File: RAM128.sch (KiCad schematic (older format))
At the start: 39 parts, among them J1 AppleIIBus, U1 621024, U10 74LS32, U11 74AHC1G126GW, U2 74HCT245, U3 74LS273, U4 74LS273, U5 74LS04, U6 74LS08, U7 74LS08, U8 74LS08, U9 74LS08

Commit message: Update docs
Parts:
- removed C12, C13, C14, C15, C16: 2u2, stdpads:C_0603, symbol Device:C_Small
- removed FID5: Fiducial, stdpads:Fiducial, symbol Mechanical:Fiducial
- removed H5: (no value), stdpads:PasteHole_1.1mm_PTH, symbol Mechanical:MountingHole_Pad
- C1: value 2u2 -> 10u; footprint stdpads:C_0805 -> stdpads:C_0603; LCSC Part (none) -> C23630
- C10, C2, C3, C4, C6, C7, C8, C9: LCSC Part (none) -> C23630
- C11: value 2u2 -> 10u; footprint stdpads:C_0603 -> stdpads:C_0805; LCSC Part (none) -> C15850
- C12: renamed from C5; value 2u2 -> 10u; LCSC Part (none) -> C15850
- R1: LCSC Part (none) -> C26010
- U1: LCSC Part (none) -> C261864
- U10: value 74LS32 -> 74HCT32; LCSC Part (none) -> C132266
- U11: LCSC Part (none) -> C7485
- U2: LCSC Part (none) -> C5980
- U3, U4: value 74LS273 -> 74HCT273; LCSC Part (none) -> C5983
- U5: value 74LS04 -> 74HCT04; LCSC Part (none) -> C131317
- U6, U7, U8, U9: value 74LS08 -> 74HCT08; LCSC Part (none) -> C8181
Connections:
- no-connect marks 7 -> 12
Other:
- moved on the sheet: C1, C10, C2, C3, C4, C6, C7, C8, C9, R1, U10B, U10C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

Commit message: Fabbed?
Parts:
- removed U2: 74HCT245, stdpads:TSSOP-20_4.4x6.5mm_P0.65mm, symbol 74xx:74HC245
- removed unit 2 of U7
- removed unit 1 of U7
- added H5: (no value), stdpads:PasteHole_1.152mm_NPTH, symbol Mechanical:MountingHole_Pad
- added U2: 74HCT245PW, stdpads:TSSOP-20_4.4x6.5mm_P0.65mm, symbol GW_Logic:74245
- added unit 1 of U7
- added unit 2 of U7
- C1: value 10u -> 2u2
- H1, H2, H3: footprint stdpads:PasteHole_1.1mm_PTH -> stdpads:PasteHole_1.152mm_NPTH
- U10: value 74HCT32 -> 74HCT32PW
- U11: value 74AHC1G126GW -> 74AHCT1G126GW
- U3, U4: value 74HCT273 -> 74HCT273PW
- U5: value 74HCT04 -> 74HCT04PW
- U6, U8, U9: value 74HCT08 -> 74HCT08PW
- U7: value 74HCT08 -> 74HCT32PW; symbol 74xx:74LS08 -> 74xx:74LS32
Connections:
- net +5V: now also U2.20 (Vcc)
- net A0: now also U6.13
- net A1: now also U6.5; no longer U6.2
- net A2: now also U7.4; no longer U6.9
- net D0: now also U2.11 (B7)
- net D1: now also U2.12 (B6)
- net D2: now also U2.13 (B5)
- net D3: now also U2.14 (B4)
- net D4: now also U2.15 (B3)
- net D5: now also U2.16 (B2)
- net D6: now also U2.17 (B1)
- net D7: now also U2.18 (B0)
- net ENWR1: now also U6.12
- net ENWR1A0: now also U6.11
- net GND: now also U6.10, U6.9, H5.1, U2.10 (GND)
- net RD0: now also U2.5 (A3)
- net RD1: now also U2.4 (A2)
- net RD2: now also U2.3 (A1)
- net RD3: now also U2.2 (A0)
- net RD4: now also U2.9 (A7)
- net RD5: now also U2.8 (A6)
- net RD6: now also U2.7 (A5)
- net RD7: now also U2.6 (A4)
- net R~CS~: now also U2.19 (~OE~)
- net ~DEVSEL~: now also U7.2, U7.5; no longer U6.10, U6.13
- net at U5.6: now also U7.1; no longer U6.12
- net at U5.4: now also U6.2; no longer U6.5
- net R~WE~ renamed R~W~
- net R~W~: now also U2.1 (AtoB)
- net ~DEV~andA2: no longer names the net of U6.8
- net ~DEV~andA2: no longer U4.11 (Cp)
- net ~DEV~and~A2~ renamed ~A2~clk
- net ~A2~clk: now also U7.6; no longer U6.11
- new net A2clk: U4.11 (Cp), U7.3
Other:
- moved on the sheet: C1, C10, C11, C12, C2, C3, C4, C6, C7, C8, C9, FID1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

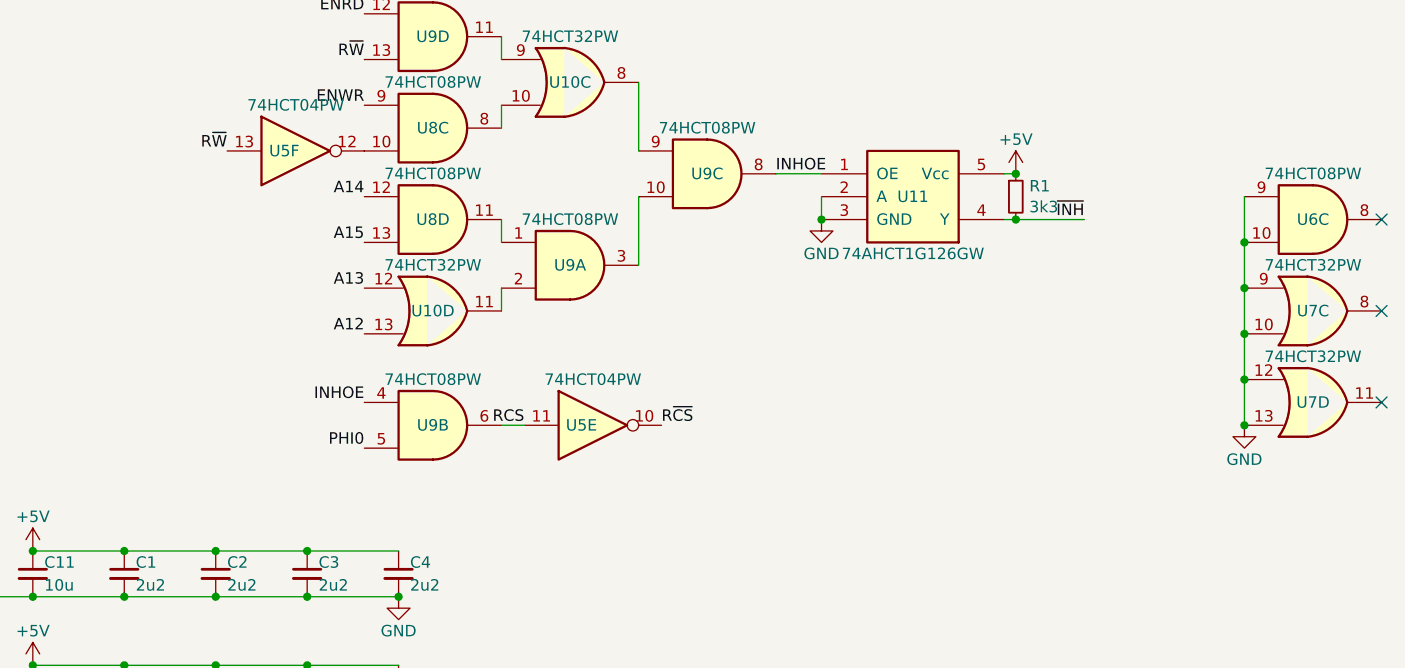
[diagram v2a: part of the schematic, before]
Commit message: DMA_OUT change
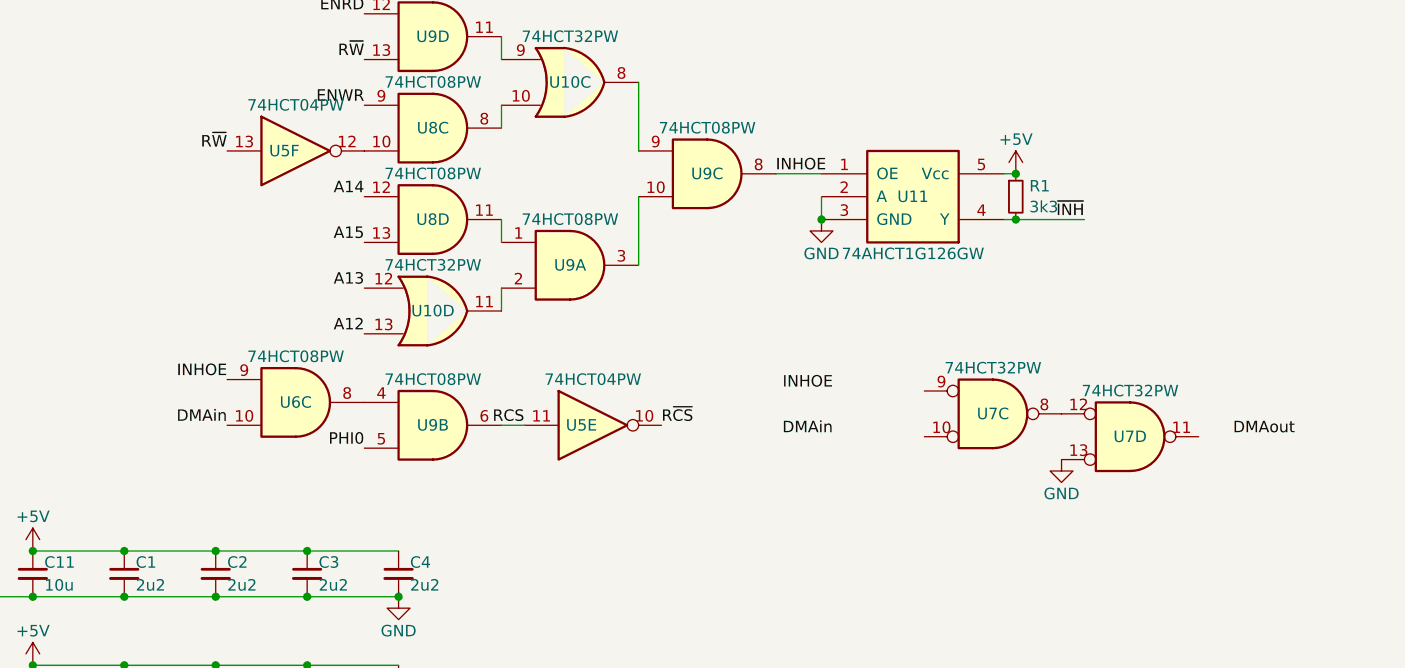
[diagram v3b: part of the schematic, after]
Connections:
- net DMAin: now also U6.10
- net GND: no longer U6.10, U6.9, U7.10, U7.12, U7.9
- net INHOE: now also U6.9; no longer U9.4
- net at U7.8: now also U7.12
- net at U6.8: now also U9.4
- no-connect marks 12 -> 9
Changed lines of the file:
@@
 Wire Bus Line
 	1850 4450 650  4450
-Text Label 8950 5300 2    50   ~ 0
-~INH~
 Text Label 5800 4600 2    50   ~ 0
 R~W~
@@
 	1    0    0    -1
 $EndComp
-Wire Wire Line
-	8650 5300 8950 5300
 $Comp
 L power:GND #PWR0126
@@
 Wire Wire Line
 	8650 5300 8600 5300
-Connection ~ 8650 5300
 $Comp
 L GW_Logic:741G126GW U11
@@
 Wire Wire Line
 	7800 5100 7600 5100
-Text Label 5800 6100 2    50   ~ 0
+Text Label 7850 6050 2    50   ~ 0
 INHOE
 Text Label 5800 5200 2    50   ~ 0
@@
 	1    0    0    -1
 $EndComp
-$Comp
-L 74xx:74LS32 U7
-U 3 1 5FD0EE1D
-P 9950 5700
-F 0 "U7" H 9950 5700 50  0000 C CNN
-F 1 "74HCT32PW" H 9950 5900 50  0000 C CNN
-F 2 "stdpads:TSSOP-14_4.4x5mm_P0.65mm" H 9950 5700 50  0001 C CNN
-F 3 "http://www.ti.com/lit/gpn/sn74LS08" H 9950 5700 50  0001 C CNN
-F 4 "C8181" H 9950 5700 50  0001 C CNN "LCSC Part"
-	3    9950 5700
-	1    0    0    -1
-$EndComp
-$Comp
-L 74xx:74LS32 U7
-U 4 1 5FD11853
-P 9950 6100
-F 0 "U7" H 9950 6100 50  0000 C CNN
-F 1 "74HCT32PW" H 9950 6300 50  0000 C CNN
-F 2 "stdpads:TSSOP-14_4.4x5mm_P0.65mm" H 9950 6100 50  0001 C CNN
-F 3 "http://www.ti.com/lit/gpn/sn74LS08" H 9950 6100 50  0001 C CNN
-F 4 "C8181" H 9950 6100 50  0001 C CNN "LCSC Part"
-	4    9950 6100
-	1    0    0    -1
-$EndComp
-$Comp
-L power:GND #PWR0127
-U 1 1 5FD15737
-P 9650 6200
-F 0 "#PWR0127" H 9650 5950 50  0001 C CNN
-F 1 "GND" H 9650 6050 50  0000 C CNN
-F 2 "" H 9650 6200 50  0001 C CNN
-F 3 "" H 9650 6200 50  0001 C CNN
-	1    9650 6200
-	1    0    0    -1
-$EndComp
-Wire Wire Line
-	9650 6200 9650 6000
-Connection ~ 9650 6200
-Connection ~ 9650 5800
-Wire Wire Line
-	9650 5800 9650 5600
-Connection ~ 9650 6000
-Wire Wire Line
-	9650 6000 9650 5800
-NoConn ~ 10250 5700
-NoConn ~ 10250 6100
 Wire Wire Line
 	8400 3050 8400 3150
@@
 	1    0    0    -1
 $EndComp
-$Comp
-L 74xx:74LS08 U6
-U 3 1 61A057BE
-P 9950 5300
-F 0 "U6" H 9950 5300 50  0000 C CNN
-F 1 "74HCT08PW" H 9950 5500 50  0000 C CNN
-F 2 "stdpads:TSSOP-14_4.4x5mm_P0.65mm" H 9950 5300 50  0001 C CNN
-F 3 "http://www.ti.com/lit/gpn/sn74LS08" H 9950 5300 50  0001 C CNN
-F 4 "C8181" H 9950 5300 50  0001 C CNN "LCSC Part"
-	3    9950 5300
-	1    0    0    -1
-$EndComp
-Wire Wire Line
-	9650 5200 9650 5400
-Wire Wire Line
-	9650 5400 9650 5600
-Connection ~ 9650 5400
-Connection ~ 9650 5600
 Wire Wire Line
 	7200 2150 7200 2350
-NoConn ~ 10250 5300
 Text Label 8000 2050 2    50   ~ 0
 ~DEVSEL~
@@
 Wire Bus Line
 	4550 2200 1750 2200
+$Comp
+L 74xx:74LS08 U6
+U 3 1 62D8945C
+P 5500 6100
+F 0 "U6" H 5500 6100 50  0000 C CNN
+F 1 "74HCT08PW" H 5500 6300 50  0000 C CNN
+F 2 "stdpads:TSSOP-14_4.4x5mm_P0.65mm" H 5500 6100 50  0001 C CNN
+F 3 "http://www.ti.com/lit/gpn/sn74LS08" H 5500 6100 50  0001 C CNN
+F 4 "C8181" H 5500 6100 50  0001 C CNN "LCSC Part"
+	3    5500 6100
+	1    0    0    -1
+$EndComp
+Text Label 5200 6200 2    50   ~ 0
+DMAin
+Text Label 9600 6250 0    50   ~ 0
+DMAout
+$Comp
+L 74xx:74LS32 U7
+U 3 2 62D952DF
+P 8550 6150
+F 0 "U7" H 8550 6150 50  0000 C CNN
+F 1 "74HCT32PW" H 8550 6350 50  0000 C CNN
+F 2 "stdpads:TSSOP-14_4.4x5mm_P0.65mm" H 8550 6150 50  0001 C CNN
+F 3 "http://www.ti.com/lit/gpn/sn74LS08" H 8550 6150 50  0001 C CNN
+F 4 "C8181" H 8550 6150 50  0001 C CNN "LCSC Part"
+	3    8550 6150
+	1    0    0    -1
+$EndComp
+$Comp
+L 74xx:74LS32 U7
+U 4 2 62D9A4DE
+P 9150 6250
+F 0 "U7" H 9150 6250 50  0000 C CNN
+F 1 "74HCT32PW" H 9150 6450 50  0000 C CNN
+F 2 "stdpads:TSSOP-14_4.4x5mm_P0.65mm" H 9150 6250 50  0001 C CNN
+F 3 "http://www.ti.com/lit/gpn/sn74LS08" H 9150 6250 50  0001 C CNN
+F 4 "C8181" H 9150 6250 50  0001 C CNN "LCSC Part"
+	4    9150 6250
+	1    0    0    -1
+$EndComp
+Connection ~ 8650 5300
+Wire Wire Line
+	8650 5300 8950 5300
+Text Label 8950 5300 2    50   ~ 0
+~INH~
+Text Label 5200 6000 2    50   ~ 0
+INHOE
+$Comp
+L power:GND #PWR?
+U 1 1 62DFF365
+P 8850 6350
+F 0 "#PWR?" H 8850 6100 50  0001 C CNN
+F 1 "GND" H 8850 6200 50  0000 C CNN
+F 2 "" H 8850 6350 50  0001 C CNN
+F 3 "" H 8850 6350 50  0001 C CNN
+	1    8850 6350
+	1    0    0    -1
+$EndComp
+Text Label 7850 6250 2    50   ~ 0
+DMAin
 Wire Bus Line
 	3150 2650 3150 3350

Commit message: done with little logic
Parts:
- removed U10, U7: 74HCT32PW, stdpads:TSSOP-14_4.4x5mm_P0.65mm, symbol 74xx:74LS32
- removed U5: 74HCT04PW, stdpads:TSSOP-14_4.4x5mm_P0.65mm, symbol 74xx:74LS04
- removed U6, U8, U9: 74HCT08PW, stdpads:TSSOP-14_4.4x5mm_P0.65mm, symbol 74xx:74LS08
- added JP1: Disable DMA Gate, Connector_PinHeader_2.54mm:PinHeader_1x02_P2.54mm_Vertical, symbol Device:Jumper_NO_Small
- added R3, R4: 30, stdpads:R_0603, symbol Device:R_Small
- added R6: 3k3, stdpads:R_0603, symbol Device:R_Small
- added U10, U15, U17, U18, U20, U25, U29, U31, U33: 742G04GW, stdpads:SOT-363, symbol GW_Logic:742G04GW
- added U12, U14, U19, U22, U23, U24, U26, U27, U28, U30, U5, U7, U9: 74LVC1G08GW, stdpads:SOT-353, symbol GW_Logic:741G02GW
- added U13, U16, U21, U32, U34, U6, U8: 74LVC1G32GW, stdpads:SOT-353, symbol GW_Logic:741G02GW
- added U35: XC6206PxxxMR, stdpads:SOT-23, symbol Regulator_Linear:XC6206PxxxMR
- R1: footprint stdpads:R_0805 -> stdpads:R_0603
- U1: footprint stdpads:TSOP-I-32_18.4x8mm_P0.5mm -> stdpads:TSOP-I-32_11.8x8mm_P0.5mm; LCSC Part C261864 -> (none)
- U11: value 74AHCT1G126GW -> 74LVC1G125GW; symbol GW_Logic:741G126GW -> GW_Logic:741G125GW
- U2: value 74HCT245PW -> 74AHC245PW; LCSC Part C426701 -> (none)
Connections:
- net +5V: now also U35.3 (VI); no longer C10.1, C2.1, C3.1, C4.1, C6.1, C7.1, C8.1, C9.1, R1.1, U1.6 (CS), U1.8 (VCC), U11.5 (Vcc), U2.20 (Vcc), U3.20 (VCC), U4.20 (VCC)
- net A0: now also U10.1 (1A), U7.1 (B), U9.2 (A); no longer U1.1 (A11)
- net A1: now also U10.3 (2A), U7.2 (A); no longer U1.2 (A9)
- net A10: now also U25.1 (1A); no longer U1.19 (A1)
- net A11: now also U25.3 (2A); no longer U1.20 (A0)
- net A12: now also U12.2 (A), U32.2 (A)
- net A13: now also U29.1 (1A), U32.1 (B); no longer U1.31 (A10)
- net A14: now also U26.1 (B)
- net A15: now also U26.2 (A)
- net A2: now also U15.1 (1A), U16.1 (B); no longer U1.3 (A8)
- net A2clk: now also U8.4 (Y)
- net A3: now also U15.3 (2A); no longer U1.4 (A13)
- net A4: now also U17.1 (1A); no longer U1.16 (A4)
- net A5: now also U17.3 (2A); no longer U1.15 (A5)
- net A6: now also U18.1 (1A); no longer U1.13 (A7)
- net A7: now also U18.3 (2A); no longer U1.7 (A15)
- net A8: now also U20.1 (1A); no longer U1.17 (A3)
- net A9: now also U20.3 (2A); no longer U1.18 (A2)
- net BankAB: now also U14.2 (A)
- net DMAin: now also U22.2 (A), U27.2 (A); no longer J1.24 (Pin_24)
- net ENRD: now also U19.1 (B)
- net ENWR: now also U23.1 (B)
- net ENWR1: now also U9.1 (B)
- net ENWR1A0: now also U9.4 (Y)
- net GND: now also R6.2, U10.2 (GND), U12.3 (GND), U13.3 (GND), U14.3 (GND), U15.2 (GND), U16.3 (GND), U17.2 (GND), U18.2 (GND), U19.3 (GND), U20.2 (GND), U21.3 (GND), U22.3 (GND), U23.3 (GND), U24.3 (GND), U25.2 (GND), U26.3 (GND), U27.3 (GND), U28.3 (GND), U29.2 (GND), U30.3 (GND), U31.2 (GND), U32.3 (GND), U33.2 (GND), U34.3 (GND), U35.1 (GND), U5.3 (GND), U6.3 (GND), U7.3 (GND), U8.3 (GND), U9.3 (GND); no longer U3.17 (D6)
- net INHOE: now also U24.4 (Y), U27.1 (B), U31.1 (1A); no longer U11.1 (OE)
- net PHI0: now also U30.2 (A)
- net RA12: now also U1.1 (A11), U13.4 (Y); no longer U1.14 (A6)
- net RA14: now also U1.16 (A4); no longer U1.12 (A12)
- net RA15: now also U1.15 (A5); no longer U1.11 (A14)
- net RA16: now also U1.14 (A6); no longer U1.10 (A16)
- net RCS: now also U30.4 (Y), U31.3 (2A)
- net R~CS~: now also U31.4 (2Y)
- net R~W~: now also U33.3 (2A); no longer U1.5 (~WE), U2.1 (AtoB)
- net ~A0XOR1~: now also U6.4 (Y)
- net ~A2~clk: now also U16.4 (Y)
- net ~DEVSEL~: now also U16.2 (A), U8.2 (A)
- net ~INH~: now also R4.1; no longer R1.2, U11.4 (Y)
- new net: R1.2, R4.2, U11.4 (Y)
- new net: U5.4 (Y), U6.2 (A)
- new net: U6.1 (B), U7.4 (Y)
- new net: U12.4 (Y), U13.2 (A)
- new net: U13.1 (B), U14.4 (Y)
- new net: U19.4 (Y), U21.1 (B)
- new net: U21.2 (A), U23.4 (Y)
- new net: U21.4 (Y), U24.1 (B)
- new net: U26.4 (Y), U28.2 (A)
- new net: U28.1 (B), U32.4 (Y)
- new net: U24.2 (A), U28.4 (Y)
- new net: U27.4 (Y), U30.1 (B)
- new net: U22.1 (B), U34.4 (Y)
- new net: R3.2, U22.4 (Y)
- new net: JP1.2, R6.1, U34.2 (A)
- new net +3V3: C10.1, C2.1, C3.1, C4.1, C6.1, C7.1, C8.1, C9.1, JP1.1, R1.1, U1.6 (CS), U1.8 (VCC), U10.5 (Vcc), U11.5 (Vcc), U12.5 (Vcc), U13.5 (Vcc), U14.5 (Vcc), U15.5 (Vcc), U16.5 (Vcc), U17.5 (Vcc), U18.5 (Vcc), U19.5 (Vcc), U2.20 (Vcc), U20.5 (Vcc), U21.5 (Vcc), U22.5 (Vcc), U23.5 (Vcc), U24.5 (Vcc), U25.5 (Vcc), U26.5 (Vcc), U27.5 (Vcc), U28.5 (Vcc), U29.5 (Vcc), U3.17 (D6), U3.20 (VCC), U30.5 (Vcc), U31.5 (Vcc), U32.5 (Vcc), U33.5 (Vcc), U34.5 (Vcc), U35.2 (VO), U4.20 (VCC), U5.5 (Vcc), U6.5 (Vcc), U7.5 (Vcc), U8.5 (Vcc), U9.5 (Vcc)
- new net DMAout: J1.24 (Pin_24), R3.1
- new net RA13: U1.2 (A9), U12.1 (B), U29.4 (2Y)
- new net RR~W~: U1.5 (~WE), U19.2 (A), U2.1 (AtoB), U33.6 (1Y)
- new net R~R~W: U23.2 (A), U33.1 (1A), U33.4 (2Y)
- new net ~A0: U1.31 (A10), U10.6 (1Y), U5.1 (B)
- new net ~A1: U1.20 (A0), U10.4 (2Y), U5.2 (A)
- new net ~A10: U1.4 (A13), U25.6 (1Y)
- new net ~A11: U1.3 (A8), U25.4 (2Y)
- new net ~A13: U14.1 (B), U29.3 (2A), U29.6 (1Y)
- new net ~A2: U1.19 (A1), U15.6 (1Y), U8.1 (B)
- new net ~A3: U1.18 (A2), U15.4 (2Y)
- new net ~A4: U1.17 (A3), U17.6 (1Y)
- new net ~A5: U1.13 (A7), U17.4 (2Y)
- new net ~A6: U1.12 (A12), U18.6 (1Y)
- new net ~A7: U1.11 (A14), U18.4 (2Y)
- new net ~A8: U1.10 (A16), U20.6 (1Y)
- new net ~A9: U1.7 (A15), U20.4 (2Y)
- new net ~INHOE~: U11.1 (~OE~), U31.6 (1Y), U34.1 (B)
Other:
- moved on the sheet: R1

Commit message: little logic done
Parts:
- added C13, C14, C15, C16, C17, C18, C19, C5: 2u2, stdpads:C_0603, symbol Device:C_Small
- added R2: 33, stdpads:R_0603, symbol Device:R_Small
- R1: LCSC Part C26010 -> C22978
- R3, R4: value 30 -> 33; LCSC Part (none) -> C23140
- R6: LCSC Part (none) -> C22978
- U1: value 621024 -> LY62W1024; LCSC Part (none) -> C261880
- U10, U15, U17, U18, U20, U25, U29, U31, U33: value 742G04GW -> 74LVC2G04GW; LCSC Part (none) -> C105251
- U12, U14, U19, U22, U23, U24, U26, U27, U28, U30, U5, U7, U9: LCSC Part (none) -> C12490
- U13, U16, U21, U32, U34, U6, U8: LCSC Part (none) -> C12489
- U2: LCSC Part (none) -> C132987
- U35: LCSC Part (none) -> C5446
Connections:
- net +3V3: now also C1.1, C13.1, C14.1, C15.1, C16.1, C17.1, C18.1, C19.1, C5.1
- net +5V: no longer C1.1
- net GND: now also C13.2, C14.2, C15.2, C16.2, C17.2, C18.2, C19.2, C5.2
- net R~CS~: now also R2.1; no longer U31.4 (2Y)
- new net: R2.2, U31.4 (2Y)
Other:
- moved on the sheet: C1, C10, C11, C12, C2, C3, C4, C6, C7, C8, C9, FID1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

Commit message: Revert "little logic done"
This reverts commit c8f7fd6b2897fba301a82931860b3ed280e7265e.
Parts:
- removed C13, C14, C15, C16, C17, C18, C19, C5: 2u2, stdpads:C_0603, symbol Device:C_Small
- removed R2: 33, stdpads:R_0603, symbol Device:R_Small
- R1: LCSC Part C22978 -> C26010
- R3, R4: value 33 -> 30; LCSC Part C23140 -> (none)
- R6: LCSC Part C22978 -> (none)
- U1: value LY62W1024 -> 621024; LCSC Part C261880 -> (none)
- U10, U15, U17, U18, U20, U25, U29, U31, U33: value 74LVC2G04GW -> 742G04GW; LCSC Part C105251 -> (none)
- U12, U14, U19, U22, U23, U24, U26, U27, U28, U30, U5, U7, U9: LCSC Part C12490 -> (none)
- U13, U16, U21, U32, U34, U6, U8: LCSC Part C12489 -> (none)
- U2: LCSC Part C132987 -> (none)
- U35: LCSC Part C5446 -> (none)
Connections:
- net +3V3: no longer C1.1
- net +5V: now also C1.1
- net R~CS~: now also U31.4 (2Y)
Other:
- moved on the sheet: C1, C10, C11, C12, C2, C3, C4, C6, C7, C8, C9, FID1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

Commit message: Revert "done with little logic"
This reverts commit 34a57e67dbc9bf65fa4ad86b3c90b017081c5d83.
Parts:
- removed JP1: Disable DMA Gate, Connector_PinHeader_2.54mm:PinHeader_1x02_P2.54mm_Vertical, symbol Device:Jumper_NO_Small
- removed R3, R4: 30, stdpads:R_0603, symbol Device:R_Small
- removed R6: 3k3, stdpads:R_0603, symbol Device:R_Small
- removed U10, U15, U17, U18, U20, U25, U29, U31, U33: 742G04GW, stdpads:SOT-363, symbol GW_Logic:742G04GW
- removed U12, U14, U19, U22, U23, U24, U26, U27, U28, U30, U5, U7, U9: 74LVC1G08GW, stdpads:SOT-353, symbol GW_Logic:741G02GW
- removed U13, U16, U21, U32, U34, U6, U8: 74LVC1G32GW, stdpads:SOT-353, symbol GW_Logic:741G02GW
- removed U35: XC6206PxxxMR, stdpads:SOT-23, symbol Regulator_Linear:XC6206PxxxMR
- added U10, U7: 74HCT32PW, stdpads:TSSOP-14_4.4x5mm_P0.65mm, symbol 74xx:74LS32
- added U5: 74HCT04PW, stdpads:TSSOP-14_4.4x5mm_P0.65mm, symbol 74xx:74LS04
- added U6, U8, U9: 74HCT08PW, stdpads:TSSOP-14_4.4x5mm_P0.65mm, symbol 74xx:74LS08
- R1: footprint stdpads:R_0603 -> stdpads:R_0805
- U1: footprint stdpads:TSOP-I-32_11.8x8mm_P0.5mm -> stdpads:TSOP-I-32_18.4x8mm_P0.5mm; LCSC Part (none) -> C261864
- U11: value 74LVC1G125GW -> 74AHCT1G126GW; symbol GW_Logic:741G125GW -> GW_Logic:741G126GW
- U2: value 74AHC245PW -> 74HCT245PW; LCSC Part (none) -> C426701
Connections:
- net DMAout is gone; now on net DMAin: J1.24 (Pin_24)
- net RA13 is gone; now on net A1: U1.2 (A9)
- net RR~W~ is gone; now on net R~W~: U1.5 (~WE), U2.1 (AtoB)
- net ~A0 is gone; now on net A13: U1.31 (A10)
- net ~A1 is gone; now on net A11: U1.20 (A0)
- net ~A10 is gone; now on net A3: U1.4 (A13)
- net ~A11 is gone; now on net A2: U1.3 (A8)
- net ~A2 is gone; now on net A10: U1.19 (A1)
- net ~A3 is gone; now on net A9: U1.18 (A2)
- net ~A4 is gone; now on net A8: U1.17 (A3)
- net ~A5 is gone; now on net A6: U1.13 (A7)
- net ~A6 is gone; now on net RA14: U1.12 (A12)
- net ~A7 is gone; now on net RA15: U1.11 (A14)
- net ~A8 is gone; now on net RA16: U1.10 (A16)
- net ~A9 is gone; now on net A7: U1.7 (A15)
- net ~INHOE~ is gone; now on net INHOE: U11.1 (OE)
- net +5V: now also C10.1, C2.1, C3.1, C4.1, C6.1, C7.1, C8.1, C9.1, R1.1, U1.6 (CS), U1.8 (VCC), U11.5 (Vcc), U2.20 (Vcc), U3.20 (VCC), U4.20 (VCC), U10.14 (VCC), U5.14 (VCC), U6.14 (VCC), U7.14 (VCC), U8.14 (VCC), U9.14 (VCC)
- net A0: now also U1.1 (A11), U5.1, U6.13, U6.4
- net A1: now also U5.3, U6.5
- net A12: now also U10.13, U8.5
- net A13: now also U10.12, U5.9, U8.4
- net A14: now also U8.12
- net A15: now also U8.13
- net A2: now also U5.5, U7.4
- net A2clk: now also U7.3
- net A4: now also U1.16 (A4)
- net A5: now also U1.15 (A5)
- net BankAB: now also U8.2
- net DMAin: now also U6.10
- net ENRD: now also U9.12
- net ENWR: now also U8.9
- net ENWR1: now also U6.12
- net ENWR1A0: now also U6.11
- net GND: now also U3.17 (D6), U10.7 (GND), U5.7 (GND), U6.7 (GND), U7.13, U7.7 (GND), U8.7 (GND), U9.7 (GND)
- net INHOE: now also U6.9, U9.8
- net PHI0: now also U9.5
- net RA12: now also U1.14 (A6), U10.6; no longer U1.1 (A11)
- net RA14: no longer U1.16 (A4)
- net RA15: no longer U1.15 (A5)
- net RA16: no longer U1.14 (A6)
- net RCS: now also U5.11, U9.6
- net R~CS~: now also U5.10
- net R~W~: now also U5.13, U9.13
- net ~A0XOR1~: now also U10.3
- net ~A2~clk: now also U7.6
- net ~DEVSEL~: now also U7.2, U7.5
- net ~INH~: now also R1.2, U11.4 (Y)
- removed net +3V3: C10.1, C2.1, C3.1, C4.1, C6.1, C7.1, C8.1, C9.1, R1.1, U1.6 (CS), U1.8 (VCC), U11.5 (Vcc), U2.20 (Vcc), U3.17 (D6), U3.20 (VCC), U4.20 (VCC)
- new net: U5.6, U7.1
- new net: U10.4, U8.3
- new net: U10.5, U8.6
- new net: U5.8, U8.1
- new net: U10.9, U9.11
- new net: U5.12, U8.10
- new net: U10.10, U8.8
- new net: U8.11, U9.1
- new net: U10.11, U9.2
- new net: U9.10, U9.3
- new net: U10.8, U9.9
- new net: U6.8, U9.4
- new net: U10.1, U6.3
- new net: U10.2, U6.6
- new net: U5.2, U6.1
- new net: U5.4, U6.2
- new net: U7.12, U7.8
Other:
- moved on the sheet: R1
